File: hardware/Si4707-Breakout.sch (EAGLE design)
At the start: 39 parts, among them J3 OUTPUT, J4 ANT, U3 TPA6111, Y1 32.768kHz

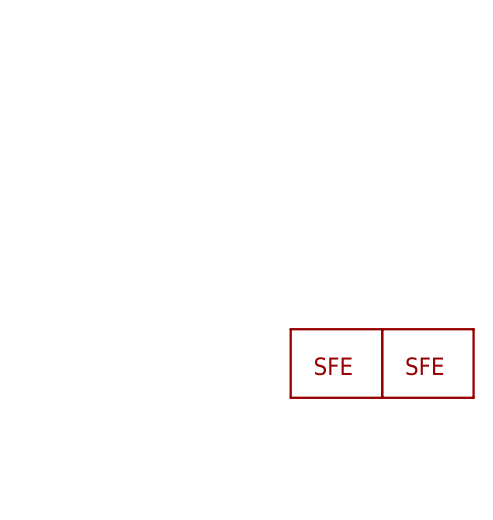
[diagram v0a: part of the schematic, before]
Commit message: Production readied
Added fiducials to design. Created production panel.
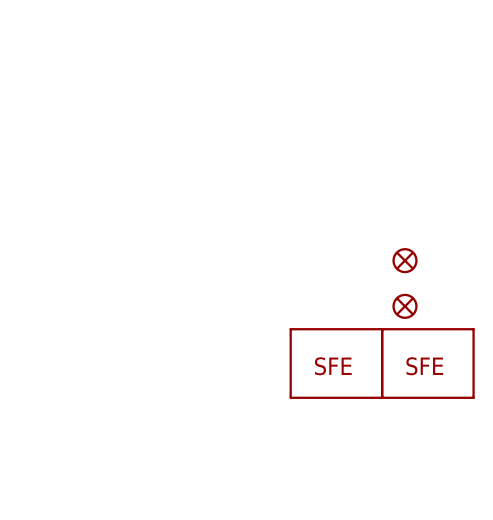
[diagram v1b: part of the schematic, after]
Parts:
- added JP4, JP5: FIDUCIALUFIDUCIAL, SparkFun:FIDUCIALUFIDUCIAL
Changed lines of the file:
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@@
 <?xml version="1.0" encoding="utf-8"?>
 <!DOCTYPE eagle SYSTEM "eagle.dtd">
-<eagle version="6.2">
+<eagle version="6.3">
 <drawing>
 <settings>
@@
 <part name="GND6" library="SparkFun-Aesthetics" deviceset="GND" device=""/>
 <part name="GND13" library="SparkFun-Aesthetics" deviceset="GND" device=""/>
+<part name="JP4" library="SparkFun" deviceset="FIDUCIAL" device="UFIDUCIAL"/>
+<part name="JP5" library="SparkFun" deviceset="FIDUCIAL" device="UFIDUCIAL"/>
 </parts>
 <sheets>
@@
 <instance part="GND6" gate="1" x="223.52" y="93.98"/>
 <instance part="GND13" gate="1" x="223.52" y="137.16"/>
+<instance part="JP4" gate="G$1" x="241.3" y="30.48"/>
+<instance part="JP5" gate="G$1" x="241.3" y="25.4"/>
 </instances>
 <busses>

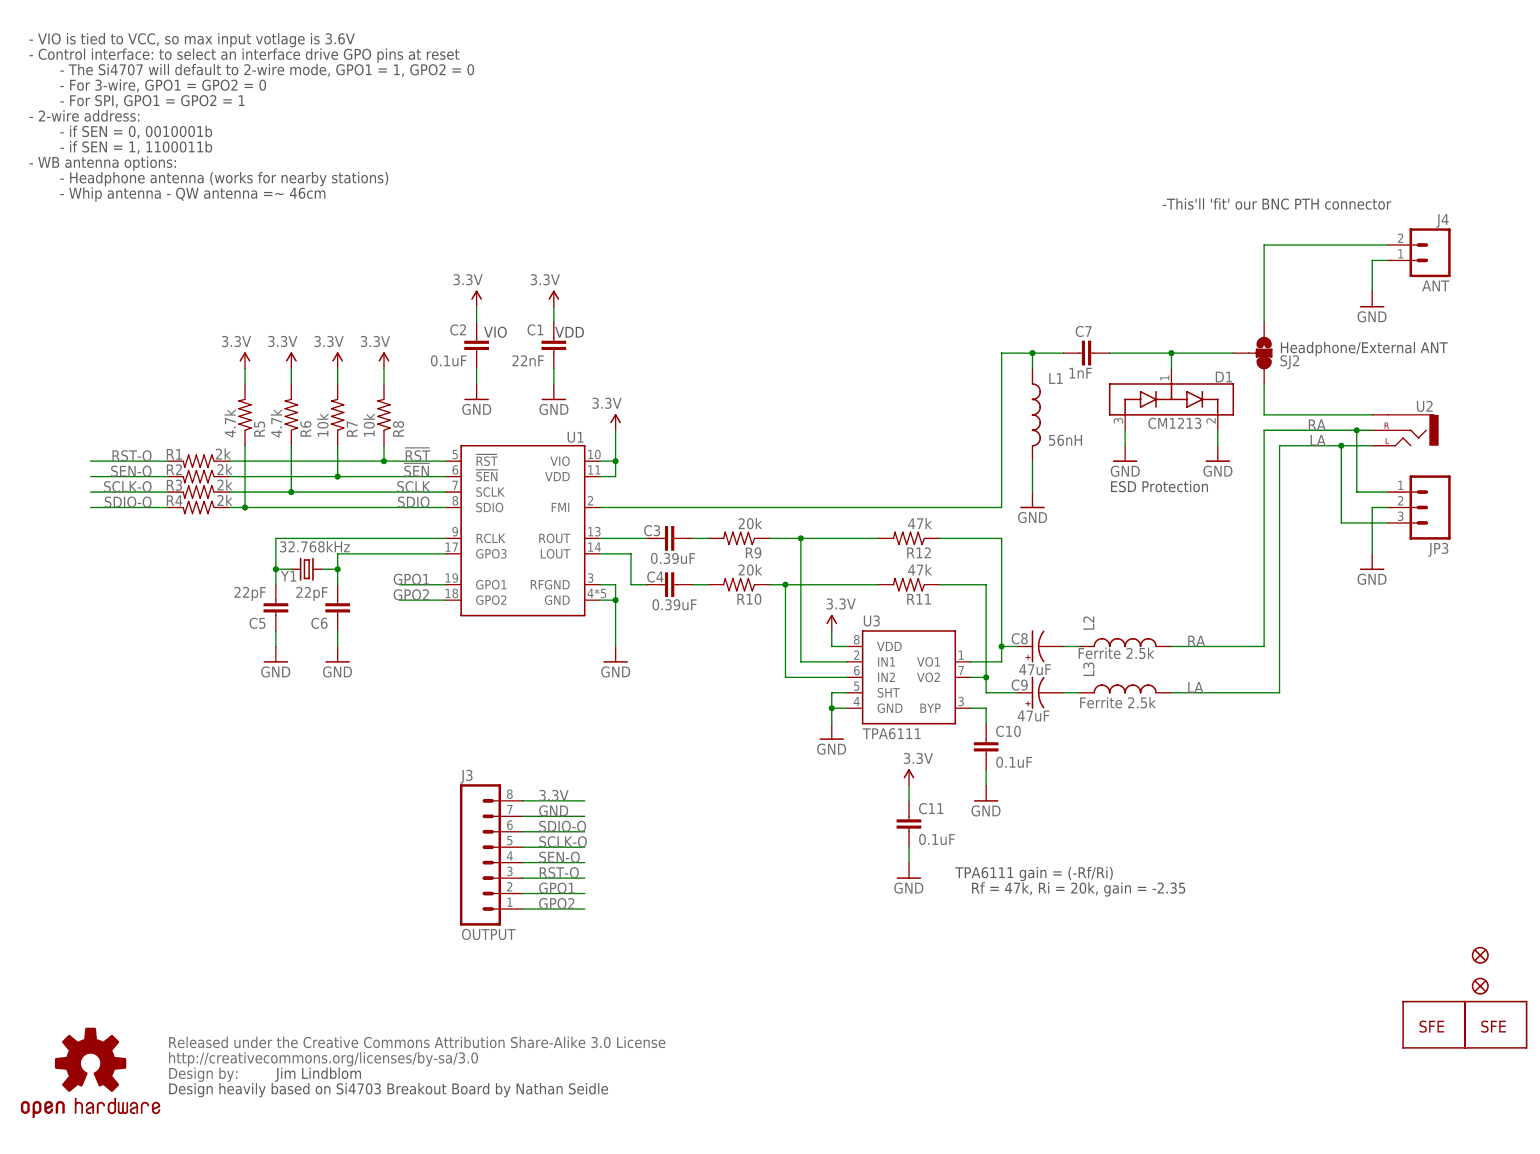
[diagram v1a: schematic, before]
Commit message: Cleaning up schematic, matching it up to release
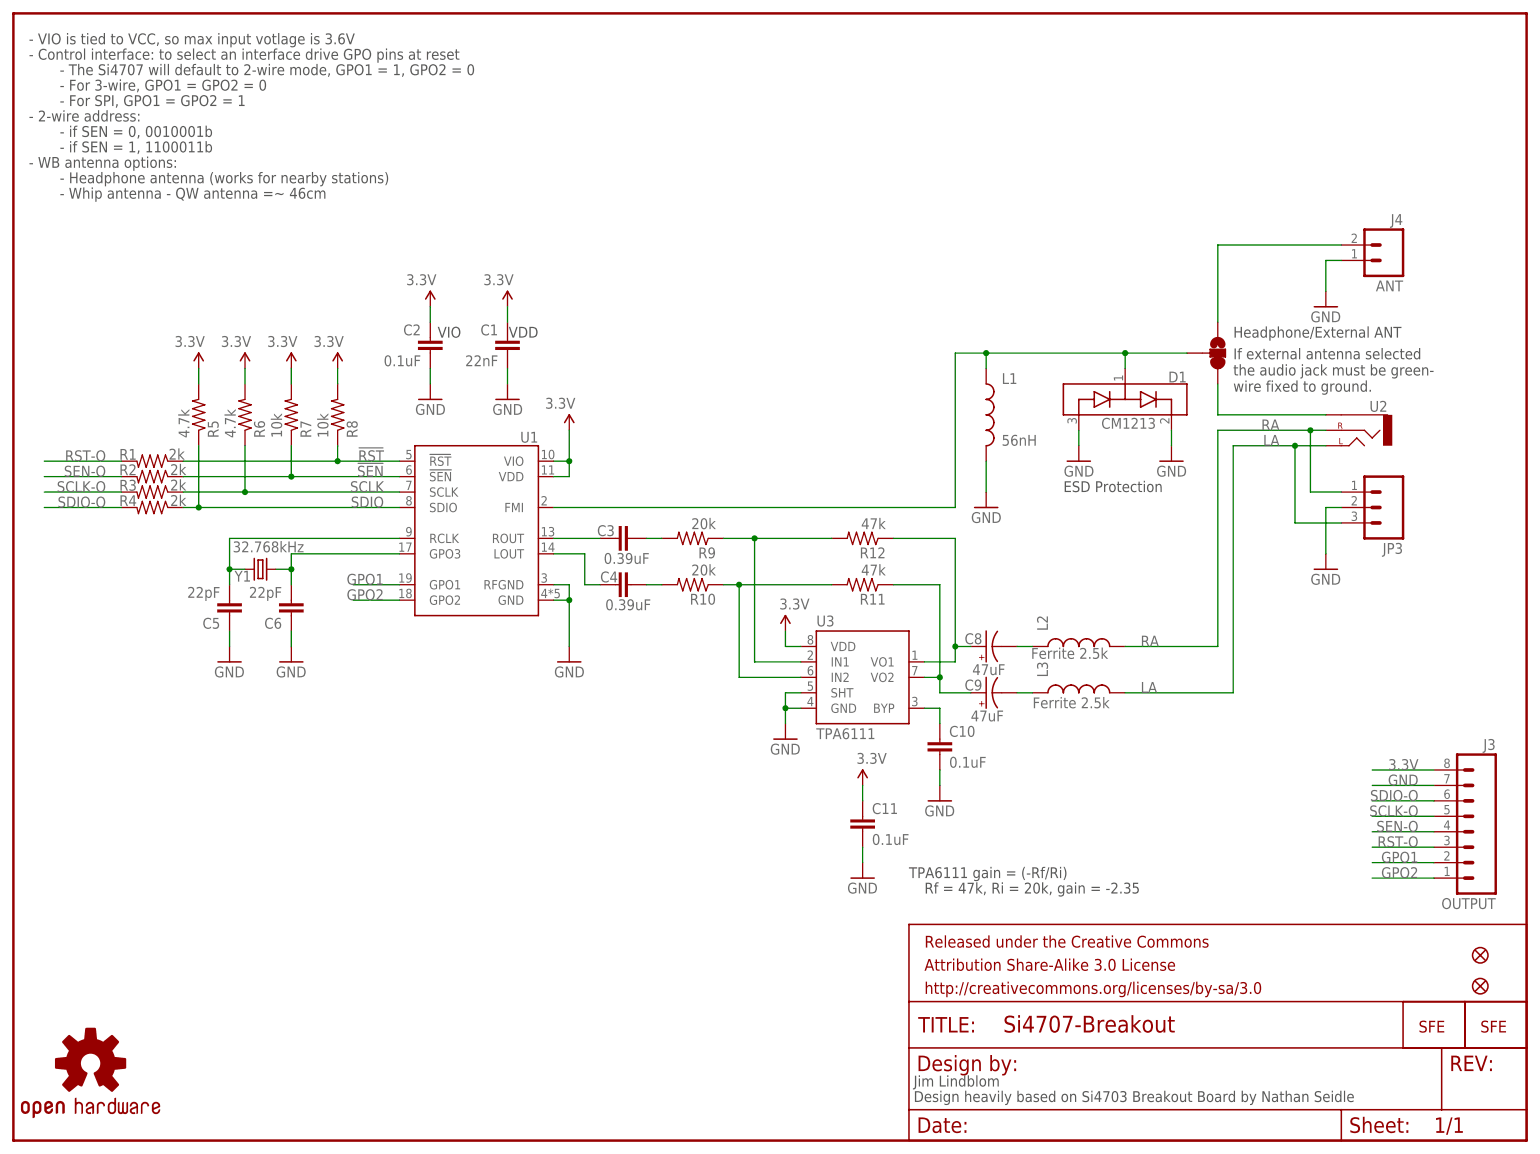
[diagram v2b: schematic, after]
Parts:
- removed C7: 1nF, SparkFun-Passives:CAP0402-CAP
- removed U$1: CREATIVE_COMMONS, SparkFun-Aesthetics:CREATIVE_COMMONS
- added FRAME1: FRAME-LETTER, SparkFun-Aesthetics:FRAME-LETTER
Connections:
- removed net N$8: C7.1, L1.1, U1.FMI
- net J1: now also L1.1, U1.FMI; no longer C7.2
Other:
- note added: "If external antenna selected the audio jack must be green- wire fixed to ground."
- note removed: "-This'll 'fit' our BNC PTH connector"
- moved on the sheet: C1, C10, C11, C2, C3, C4, C5, C6, C8, C9, D1, J3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
